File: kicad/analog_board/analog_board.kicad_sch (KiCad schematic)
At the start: 74 parts

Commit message: Приступил к переосмыслению схемы аналоговой платы.
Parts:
- removed C12, C16, C17, C18, C19, C20, C21: 0.1 мк, IWsmd_case:SMD0805, symbol LFcapitors:CAPITORS
- removed C13, C14: 220 мк 25 В, IWcomponents:CAPACITOR_3_D8, symbol LFcapitors:CAPITORS_ELECTROLYTIC
- removed C15: 470 мк 16 В, IWcomponents:CAPACITOR_3_D8, symbol LFcapitors:CAPITORS_ELECTROLYTIC
- removed C3: 1 мк 305 В, IWcomponents:CAPACITOR_B32923_26.5x11, symbol LFcapitors:CAPITORS
- removed C7: 4700 мк 16 В, IWcomponents:CAPACITOR_7.62_D16, symbol LFcapitors:CAPITORS_ELECTROLYTIC
- removed C8, C9: 2200 мк 35 В, IWcomponents:CAPACITOR_7.62_D16, symbol LFcapitors:CAPITORS_ELECTROLYTIC
- removed DA3: LM317, IWcomponents:TO220_RAD_16.5x15, symbol LFcomponents:LM317
- removed DA4: LM317T, IWcomponents:TO220_RAD_16.5x15, symbol LFcomponents:LM317
- removed DA5: LM337T, IWcomponents:TO220_RAD_16.5x15, symbol LFcomponents:LM337
- removed DA6: AD680AR, IWsmd_case:SOIC8, symbol LFcomponents:AD680AR
- removed DA7: OP07CD, IWsmd_case:SOIC8, symbol LFcomponents:OP07
- removed FU1: 0.1A, IWcomponents:FU_PTF15B, symbol LFcomponents:PROTECTOR
- removed LL1: B82731T2301A020, IWtransformator:EMI_EPCOS_B82731T, symbol LFtransformator:CHOKES_PL
- removed R12, R2: 10 к, IWcomponents:Electron_3296W, symbol LFresistor:RESISTOR_TRIMMING
- removed R14, R16, R17: 5 к, IWcomponents:Electron_3296W, symbol LFresistor:RESISTOR_TRIMMING
- removed R19, R22, R23, R24: 100 к, IWsmd_case:SMD0805, symbol LFresistor:RESISTOR
- removed R3: 15 к, IWsmd_case:SMD0805, symbol LFresistor:RESISTOR
- removed R5: 3.3 к, IWsmd_case:SMD0805, symbol LFresistor:RESISTOR
- removed R6: 510 к, IWsmd_case:SMD2512, symbol LFresistor:RESISTOR
- removed RU1: B72210S0271K101, IWcomponents:RU_EPCOS_B72210S0271K101_12х5, symbol LFresistor:VARISTOR
- removed TV1: ТПК-2 (6В), IWtransformator:TPG2-12, symbol LFtransformator:TPG-112-12
- removed TV2: ТП-112-11 (2х15В), IWtransformator:TP112-11, symbol LFtransformator:TP-112-11
- removed VD1, VD10, VD11, VD2, VD3, VD4, VD5, VD6, VD7, VD8, VD9: VS-10MQ100NTRPBF, IWcomponents:SMA, symbol LFdiod:SHOTTKY_DIODE
- removed XP3, XP4: L-KLS8-01128-PC-250-0.8, IWconnectors:TERMINAL_KLS8-01128_6.3mm, symbol LFconnectors:connector_1pin_gost
- removed XP5: WF-3, IWconnectors:WF-3, symbol LFconnectors:connector_3pin_gost
- added C8, C9: 0.1 мк, IWsmd_case:SMD0805, symbol LFcapitors:CAPITORS
- added DA1: TL431B, symbol LFcomponents:TL431x_sot23
- added DA4: OP177GSZ, IWsmd_case:SOIC8, symbol LFcomponents:OP07
- added K1, K2: HFD4/5-LSR, symbol IWrelays:HFD4xx-SR
- added R1, R2: 1 к, IWsmd_case:SMD0805, symbol LFresistor:RESISTOR
- added R11: 3.3 к, IWsmd_case:SMD0805, symbol LFresistor:RESISTOR
- added R12: 1.5 к, IWsmd_case:SMD0805, symbol LFresistor:RESISTOR
- added R14, R16: 10 к, IWsmd_case:SMD0805, symbol LFresistor:RESISTOR
- added R22: 20 к, IWcomponents:Electron_3296W, symbol LFresistor:RESISTOR_TRIMMING
- added R4: 50, IWsmd_case:SMD0805, symbol LFresistor:RESISTOR
- added R5: 2 к, IWcomponents:Electron_3296W, symbol LFresistor:RESISTOR_TRIMMING
- added R8: 20 к, IWsmd_case:SMD0805, symbol LFresistor:RESISTOR
- added VD1: KC168, symbol LFdiod:STABILITRON
- added VD2, VD3: 1N4007, symbol LFdiod:DIODE
- added VT1, VT2, VT3: MMBT5551, symbol LFtransistor:NPN
- added XP3: WF-2, IWconnectors:WF-2, symbol LFconnectors:connector_3pin_gost
- C1: value 1 мк 305 В -> 1 мк; footprint IWcomponents:CAPACITOR_B32923_26.5x11 -> IWsmd_case:SMD0805
- DA3: renamed from DA2; value OP07CD -> OP177GSZ
- R13: value 240 -> 810
- R15, R18: value 240 -> 1 к
- R17: renamed from R10; value 10 к -> 5.1 к
- R19: renamed from R11; value 10 к -> 5.1 к
- R20, R21: value 100 к -> 1 к
- R3: renamed from R1; value 50 -> 0
- R6: renamed from R8; value 15 к -> 20 к
- R9: value 0 -> 200 к
- renumbered C4 to C3, C5 to C4, C6 to C5, C10 to C6, C11 to C7, DA1 to DA2, R4 to R10, XP6 to XP5
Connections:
- net +5V: now also R3.2, K1.8, K2.8, R14.1, R16.1, R2.1, VD2.2, VD3.2, XP3.3; no longer R13.2
- net AGND: now also C1.1, R20.2, R8.1, VD1.1; no longer R21.1
- net GND: now also C8.2, C9.2, DA1.3 (A), R5.1, VT2.1, VT3.1; no longer XP1.4
- net SIG_OUT: now also DA4.6, R22.1
- net at DA2.1 (Rg): now also R13.1, R11.1, R12.1
- net at DA2.3, XP1.1: now also R9.2
- net at DA2.6: now also R17.1; no longer R9.2
- net at DA2.8 (Rg): now also K2.3, K2.6
- net at DA3.2: now also C4.1, DA3.6, DA4.3
- net at R7.3: now also R8.2
- net at R9.1: now also C1.2, R6.2, R1.2, VD1.2; no longer R17.1
- net at R20.1: now also R21.1, DA4.2
- net at R21.2: now also R22.2, R22.3
- net at R15.1: now also R14.2, XP3.1
- net at R18.1: now also R16.2, XP3.2
- net +15V renamed +12V
- net +12V: now also C8.1, DA4.7 (V+), R1.1; no longer R15.2
- net -15V renamed -12V
- net -12V: now also C9.1, DA4.4 (V-); no longer R18.2, R6.2
- new net: VT1.3, XP1.4
- new net: DA1.1 (REF), R4.1, VT1.1
- new net: DA1.2 (C), R2.2, VT1.2
- new net: K1.1, VD2.1, VT2.3
- new net: R4.2, R5.2, R5.3
- new net: K2.2, K2.7, R11.2
- new net: R15.2, VT2.2
- new net: K2.1, VD3.1, VT3.3
- new net: K1.2, K1.7, R12.2
- new net: R18.2, VT3.2
- new net: K1.3, K1.6, K2.4, K2.5
- new net: K1.4, K1.5, R13.2
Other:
- added sheet PS_shema (PS_shema.kicad_sch)
- note added: "*(1 MOm)"
- note added: "*(100 кOm)"
- note added: "*(50 кOm)"
- note added: "+12 В"
- note added: "-12 В"
- note added: "G=(49.4 кОм / Rg) + 1 при R5 = 3.3 кОм, G = 15.97, при R5 = 1.5 кОм, G = 33.93, при R5 = 810 Ом, G = 62.99"
- note added: "K1"
- note added: "K2"
- note added: "Попробовать увеличить номиналы резисторов для уменьшения тока через фотодиод"
- note added: "Фильтр низкик частот f-6дБ = 430 Гц, f0дБ = 312 Гц"
- note removed: "+15 В"
- note removed: "-15 В"
- note removed: "220В 50Гц"
- note removed: "G=(49.4 кОм / R5) +1 при R5 = 3.3 кОм, G = 15.97, при R5 = 1.5 кОм, G = 33.93, при R5 = 810 Ом, G = 62.99"
- note removed: "Фильтр низкик частот f-6дБ = 220 Гц, f0дБ = 160 Гц"
- moved on the sheet: C2, C3, C4, C5, C6, C7, DA2, DA3, R10, R17, R19, R3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

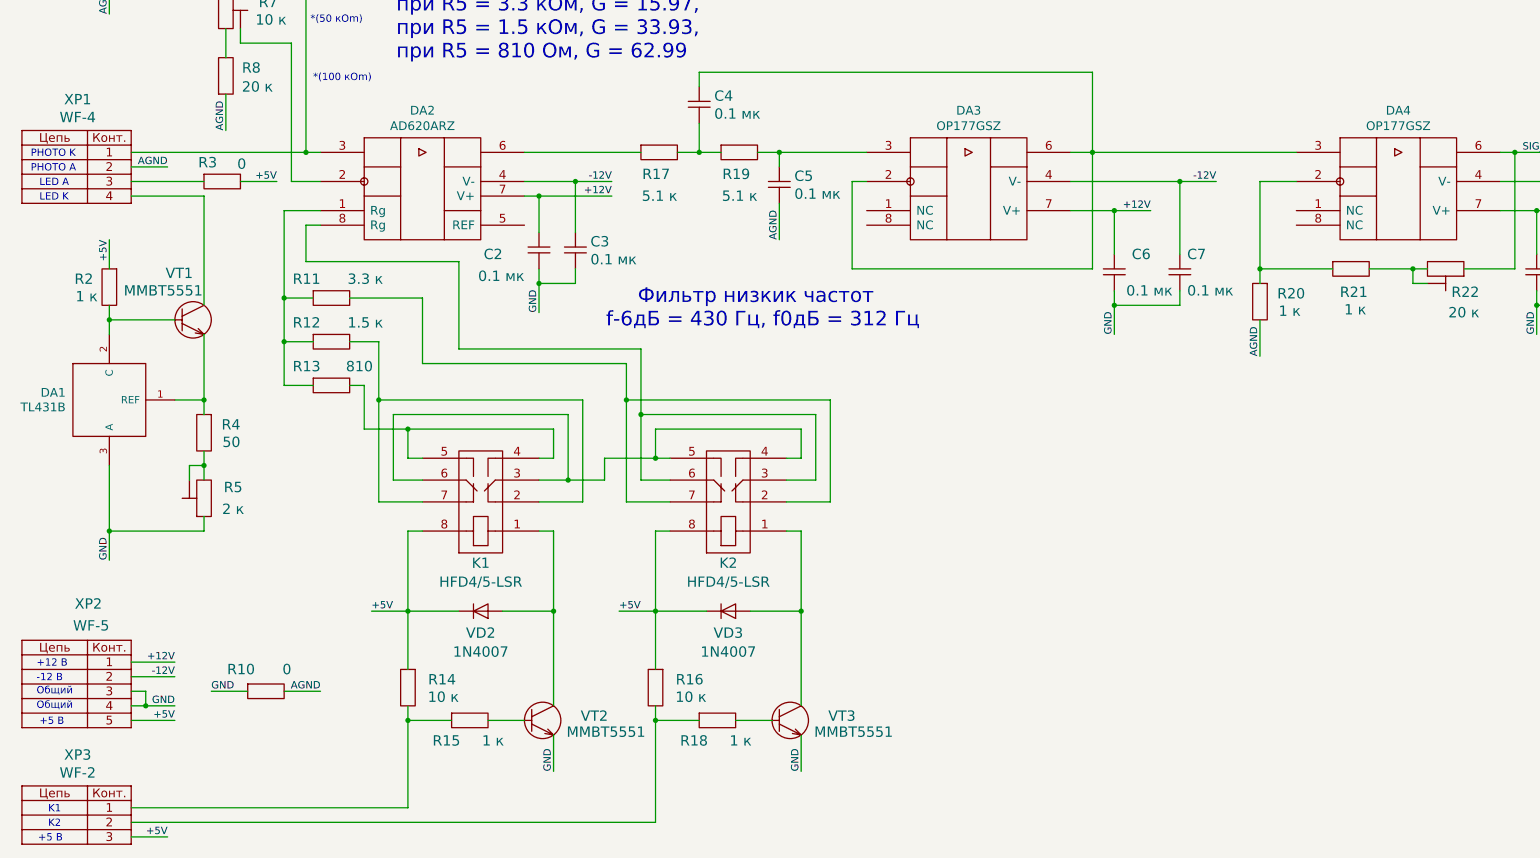
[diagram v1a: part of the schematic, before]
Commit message: Добавил новую схему усилителя для фотодиода.
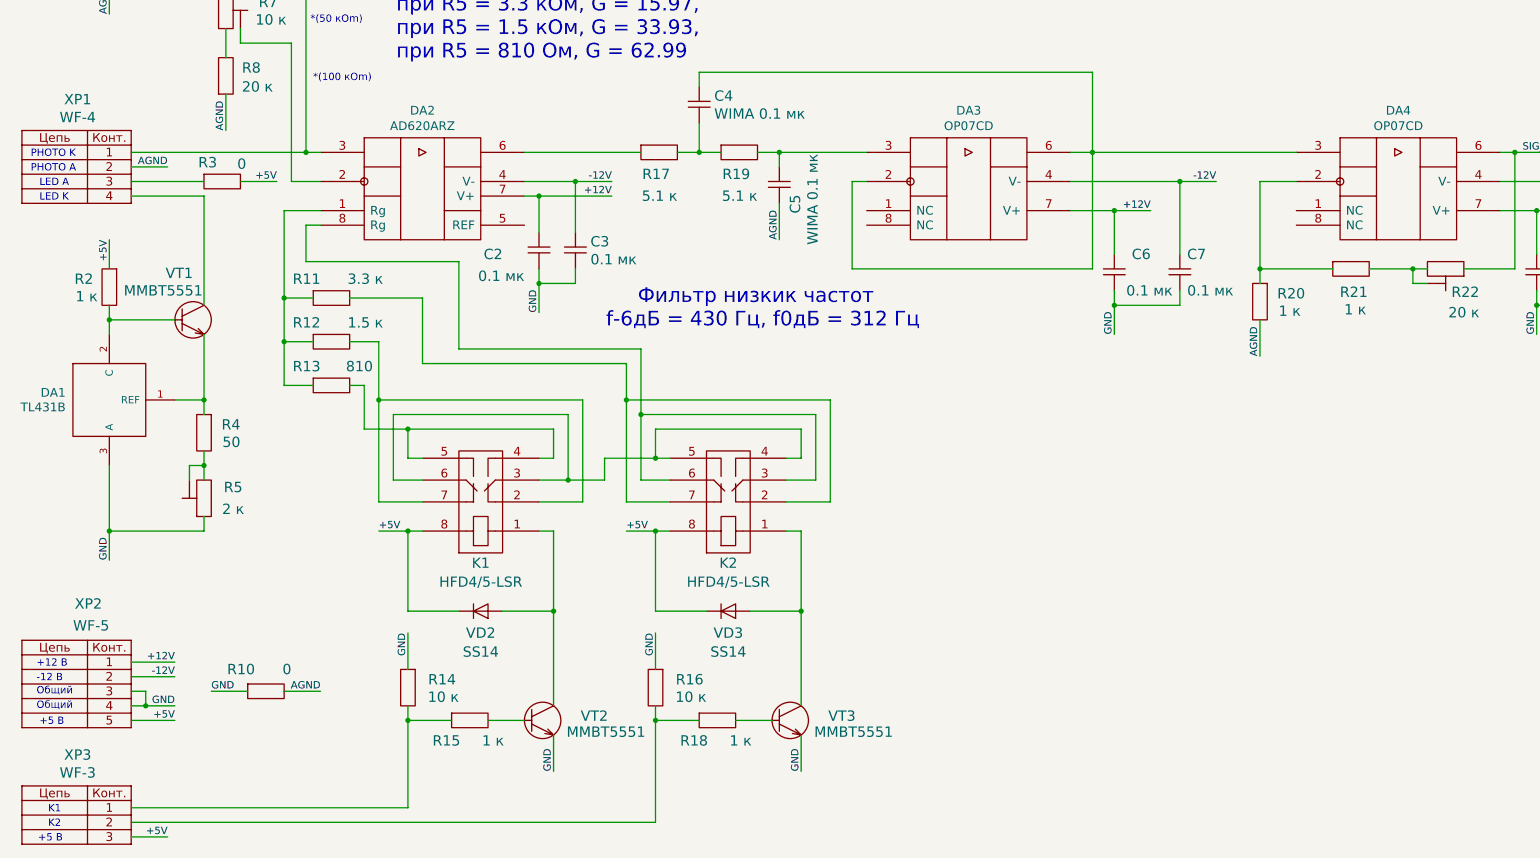
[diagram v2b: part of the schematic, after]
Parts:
- C4, C5: value 0.1 мк -> WIMA 0.1 мк
- DA3, DA4: value OP177GSZ -> OP07CD
- VD2, VD3: value 1N4007 -> SS14
- XP3: value WF-2 -> WF-3
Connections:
- net +5V: no longer R14.1, R16.1
- net GND: now also R14.1, R16.1
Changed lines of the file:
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@@
 	)
 	(junction
-		(at 92.71 154.94)
+		(at 130.81 118.11)
 		(diameter 0)
 		(color 0 0 0 0)
 	)
 	(junction
-		(at 130.81 118.11)
+		(at 135.89 128.27)
 		(diameter 0)
 		(color 0 0 0 0)
 	)
 	(junction
-		(at 135.89 128.27)
+		(at 215.9 101.6)
 		(diameter 0)
 		(color 0 0 0 0)
 	)
 	(junction
-		(at 215.9 101.6)
+		(at 135.89 140.97)
 		(diameter 0)
 		(color 0 0 0 0)
@@
 	)
 	(junction
+		(at 92.71 140.97)
+		(diameter 0)
+		(color 0 0 0 0)
+	)
+	(junction
 		(at 349.25 58.42)
 		(diameter 0)
@@
 	)
 	(junction
-		(at 135.89 154.94)
-		(diameter 0)
-		(color 0 0 0 0)
-	)
-	(junction
 		(at 57.15 118.11)
 		(diameter 0)
@@
 	(wire
 		(pts
-			(xy 129.54 154.94) (xy 135.89 154.94)
-		)
-		(stroke
-			(width 0)
-			(type default)
-		)
-	)
-	(wire
-		(pts
 			(xy 135.89 140.97) (xy 138.43 140.97)
 		)
@@
 	(wire
 		(pts
-			(xy 92.71 154.94) (xy 92.71 165.1)
-		)
-		(stroke
-			(width 0)
-			(type default)
-		)
-	)
-	(wire
-		(pts
 			(xy 138.43 128.27) (xy 135.89 128.27)
 		)
@@
 	(wire
 		(pts
+			(xy 135.89 158.75) (xy 135.89 165.1)
+		)
+		(stroke
+			(width 0)
+			(type default)
+		)
+	)
+	(wire
+		(pts
 			(xy 71.12 85.09) (xy 71.12 100.33)
 		)
@@
 	(wire
 		(pts
-			(xy 86.36 154.94) (xy 92.71 154.94)
-		)
-		(stroke
-			(width 0)
-			(type default)
-		)
-	)
-	(wire
-		(pts
 			(xy 60.96 53.34) (xy 60.96 58.42)
 		)
@@
 	(wire
 		(pts
+			(xy 87.63 140.97) (xy 92.71 140.97)
+		)
+		(stroke
+			(width 0)
+			(type default)
+		)
+	)
+	(wire
+		(pts
 			(xy 57.15 82.55) (xy 57.15 101.6)
 		)
@@
 	(wire
 		(pts
+			(xy 92.71 158.75) (xy 92.71 165.1)
+		)
+		(stroke
+			(width 0)
+			(type default)
+		)
+	)
+	(wire
+		(pts
 			(xy 40.64 33.02) (xy 40.64 35.56)
 		)
@@
 	(wire
 		(pts
+			(xy 130.81 140.97) (xy 135.89 140.97)
+		)
+		(stroke
+			(width 0)
+			(type default)
+		)
+	)
+	(wire
+		(pts
 			(xy 157.48 83.82) (xy 157.48 90.17)
 		)
@@
 	(wire
 		(pts
-			(xy 135.89 154.94) (xy 135.89 165.1)
-		)
-		(stroke
-			(width 0)
-			(type default)
-		)
-	)
-	(wire
-		(pts
 			(xy 215.9 92.71) (xy 215.9 85.09)
 		)
@@
 		)
 	)
+	(label "GND"
+		(at 135.89 158.75 270)
+		(effects
+			(font
+				(size 1.27 1.27)
+			)
+			(justify right bottom)
+		)
+	)
 	(label "+5V"
 		(at 52.07 173.99 180)
@@
 	)
 	(label "+5V"
-		(at 86.36 154.94 0)
+		(at 87.63 140.97 0)
 		(effects
 			(font
@@
 	)
 	(label "GND"
+		(at 92.71 158.75 270)
+		(effects
+			(font
+				(size 1.27 1.27)
+			)
+			(justify right bottom)
+		)
+	)
+	(label "GND"
 		(at 115.57 102.87 90)
 		(effects
@@
 	)
 	(label "+5V"
-		(at 129.54 154.94 0)
+		(at 130.81 140.97 0)
 		(effects
 			(font
@@
 			)
 		)
-		(property "Value" "OP177GSZ"
+		(property "Value" "OP07CD"
 			(at 190.5 70.3326 0)
 			(effects
@@
 			)
 		)
-		(property "Value" "0.1 мк"
+		(property "Value" "WIMA 0.1 мк"
 			(at 146.1262 68.2244 90)
 			(effects
@@
 		(dnp no)
 		(property "Reference" "C5"
-			(at 160.0962 79.0702 90)
+			(at 160.274 82.296 0)
 			(effects
 				(font
@@
 			)
 		)
-		(property "Value" "0.1 мк"
-			(at 160.0962 82.1944 90)
+		(property "Value" "WIMA 0.1 мк"
+			(at 163.322 75.184 0)
 			(effects
 				(font
@@
 			)
 		)
-		(property "Value" "1N4007"
+		(property "Value" "SS14"
 			(at 105.41 162.052 0)
 			(effects
@@
 			)
 		)
-		(property "Value" "1N4007"
+		(property "Value" "SS14"
 			(at 148.59 162.052 0)
 			(effects
@@
 			)
 		)
-		(property "Value" "OP177GSZ"
+		(property "Value" "OP07CD"
 			(at 265.43 70.3326 0)
 			(effects
@@
 			)
 		)
-		(property "Value" "WF-2"
+		(property "Value" "WF-3"
 			(at 35.1282 183.134 0)
 			(effects
